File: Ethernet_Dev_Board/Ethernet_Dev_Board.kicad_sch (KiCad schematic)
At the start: 27 parts, among them J3 Power In, J4 5V, J5 3.3V, J6 3.3VA, J7 3.3VD, U3 AZ1117

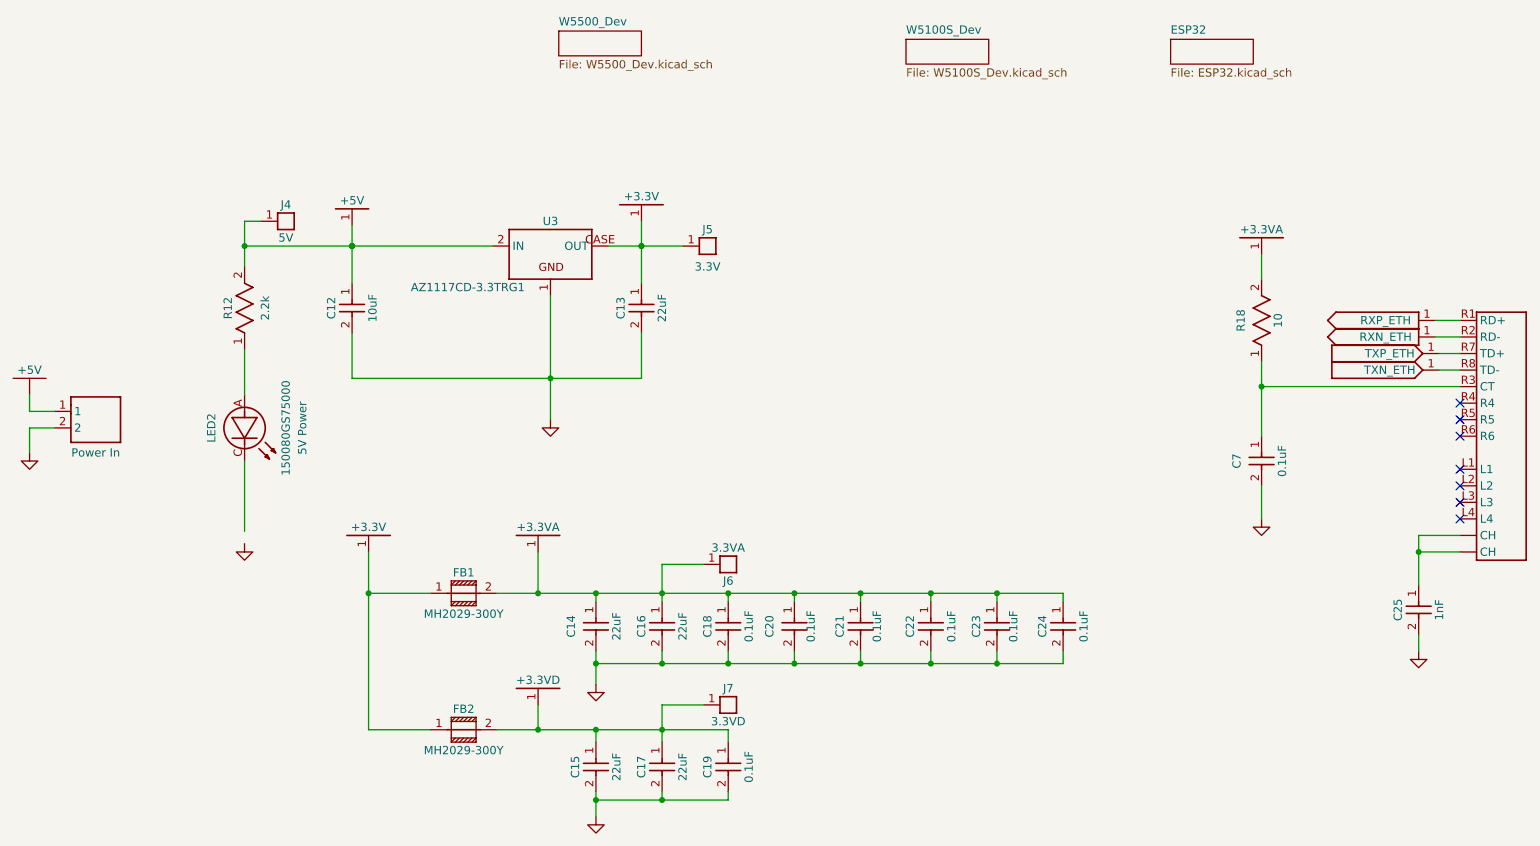
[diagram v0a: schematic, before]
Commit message: Added additional oscillator circuit. Re-annotated schematic
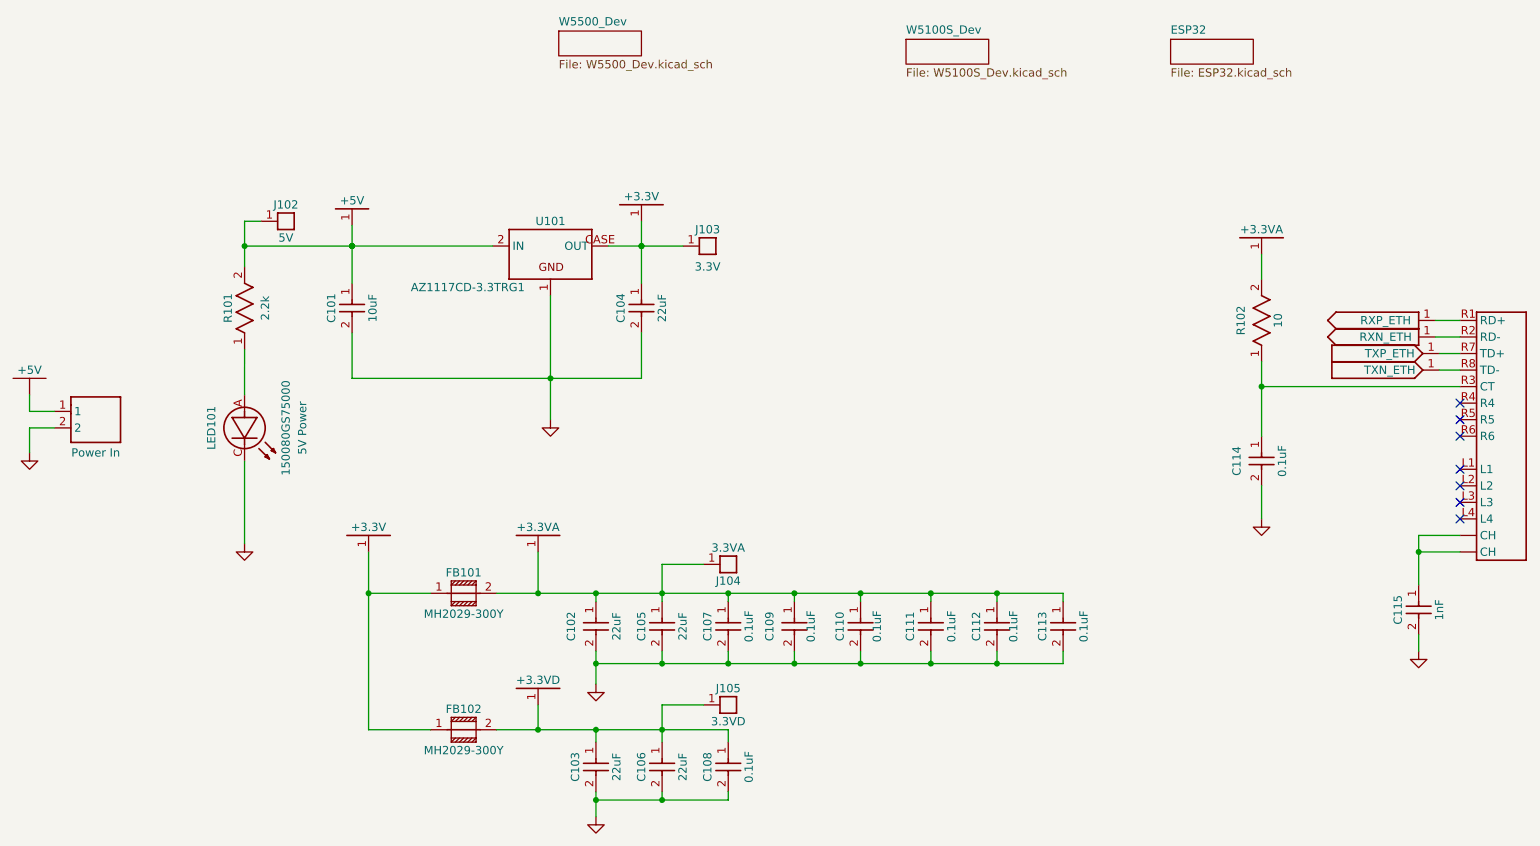
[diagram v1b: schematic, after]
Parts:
- renumbered C12 to C101, C14 to C102, C15 to C103, C13 to C104, C16 to C105, C17 to C106, C18 to C107, C19 to C108, C20 to C109, C21 to C110, C22 to C111, C23 to C112, C24 to C113, C7 to C114, C25 to C115, FB1 to FB101, FB2 to FB102, J3 to J101, J4 to J102, J5 to J103, J6 to J104, J7 to J105, J2 to J106, LED2 to LED101, R12 to R101, R18 to R102, U3 to U101
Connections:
- net GND1: now also LED101.C
